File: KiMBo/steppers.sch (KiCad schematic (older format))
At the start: 22 parts

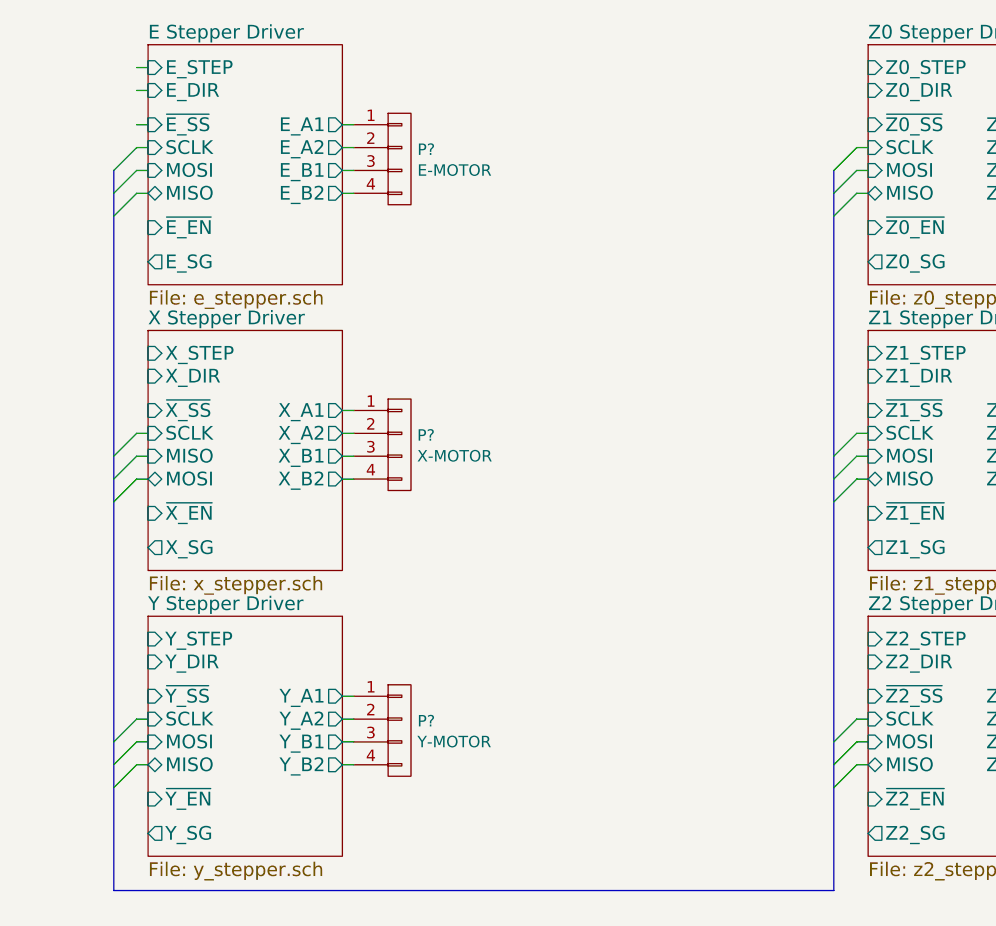
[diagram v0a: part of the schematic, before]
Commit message: Update to use OSD335x as the main chipset
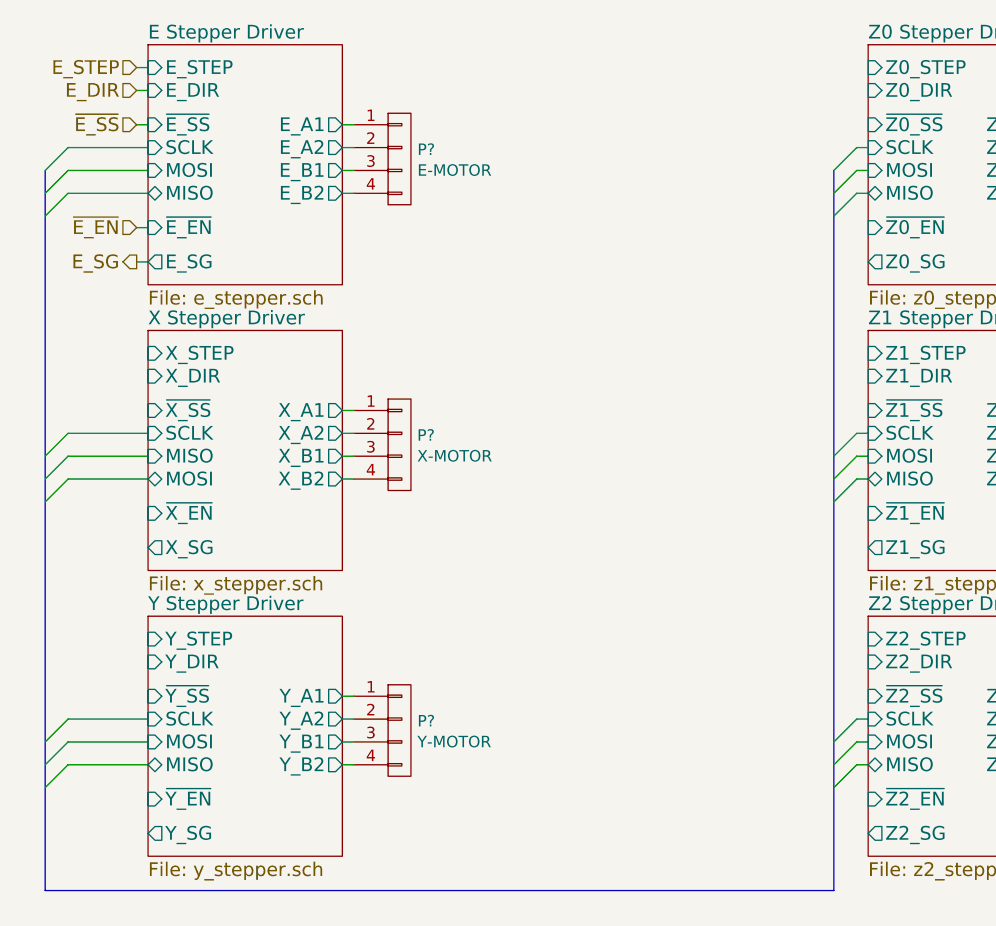
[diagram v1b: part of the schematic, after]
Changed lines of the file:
@@
 $EndSheet
 Wire Bus Line
-	2550 4600 5700 4600
+	2250 4600 5700 4600
 Wire Bus Line
 	5700 4600 5700 1450
 Entry Wire Line
-	2650 1550 2550 1650
-Entry Wire Line
-	2650 1350 2550 1450
-Entry Wire Line
-	2650 1450 2550 1550
-Wire Wire Line
-	2650 1350 2700 1350
-Wire Wire Line
-	2650 1450 2700 1450
+	2350 1550 2250 1650
+Entry Wire Line
+	2350 1350 2250 1450
+Entry Wire Line
+	2350 1450 2250 1550
+Wire Wire Line
+	2350 1350 2700 1350
+Wire Wire Line
+	2350 1450 2700 1450
 Entry Wire Line
 	5800 1350 5700 1450
@@
 	5850 1550 5800 1550
 Entry Wire Line
-	2650 2600 2550 2700
-Entry Wire Line
-	2650 2700 2550 2800
-Entry Wire Line
-	2650 2800 2550 2900
-Entry Wire Line
-	2650 3850 2550 3950
-Entry Wire Line
-	2650 3950 2550 4050
-Entry Wire Line
-	2650 4050 2550 4150
+	2350 2600 2250 2700
+Entry Wire Line
+	2350 2700 2250 2800
+Entry Wire Line
+	2350 2800 2250 2900
+Entry Wire Line
+	2350 3850 2250 3950
+Entry Wire Line
+	2350 3950 2250 4050
+Entry Wire Line
+	2350 4050 2250 4150
 Entry Wire Line
 	5800 3850 5700 3950
@@
 	5800 2800 5700 2900
 Wire Wire Line
-	2650 2600 2700 2600
-Wire Wire Line
-	2650 2700 2700 2700
-Wire Wire Line
-	2650 2800 2700 2800
-Wire Wire Line
-	2650 3850 2700 3850
-Wire Wire Line
-	2650 3950 2700 3950
-Wire Wire Line
-	2650 4050 2700 4050
+	2350 2600 2700 2600
+Wire Wire Line
+	2350 2700 2700 2700
+Wire Wire Line
+	2350 2800 2700 2800
+Wire Wire Line
+	2350 3850 2700 3850
+Wire Wire Line
+	2350 3950 2700 3950
+Wire Wire Line
+	2350 4050 2700 4050
 Wire Wire Line
 	5800 3850 5850 3850
@@
 	5800 2800 5850 2800
 Wire Wire Line
-	2650 1550 2700 1550
+	2350 1550 2700 1550
 Wire Bus Line
-	2550 1450 2550 4600
+	2250 1450 2250 4600
 $Comp
 L CONN_01X04 P?
@@
 	11400 3750 11400 3950
 Connection ~ 11400 3900
+Text HLabel 2650 1000 0    60   Input ~ 0
+E_STEP
+Text HLabel 2650 1100 0    60   Input ~ 0
+E_DIR
+Text HLabel 2650 1250 0    60   Input ~ 0
+~E_SS
+Wire Wire Line
+	2700 1700 2650 1700
+Text HLabel 2650 1700 0    60   Input ~ 0
+~E_EN
+Text HLabel 2650 1850 0    60   Output ~ 0
+E_SG
+Wire Wire Line
+	2700 1850 2650 1850
 $EndSCHEMATC

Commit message: Add eMMC to the schematic
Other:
- note added: "Potential Motor MUX Setup"
- moved on the sheet: P?
